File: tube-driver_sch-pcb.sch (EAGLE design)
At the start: 119 parts, among them CN1 KS 54, CN2 MINI B USB, CN3 KS 54, CN4 KS 54, CN5 KS 54, CN6 KS 54, CN7 KS 54, CN8 KS 54, CN9 KS 54, Q4 MMBT3904, Q5 MMBT3904, SW1 RA SM TACT, U1 CP2102, U10 TPS61500, U11 3.3V BUCK, U2 TPS61500, U3 TPS61500, U5 ESP32, U6 USBLC6-2SC6, U8 TPS61500

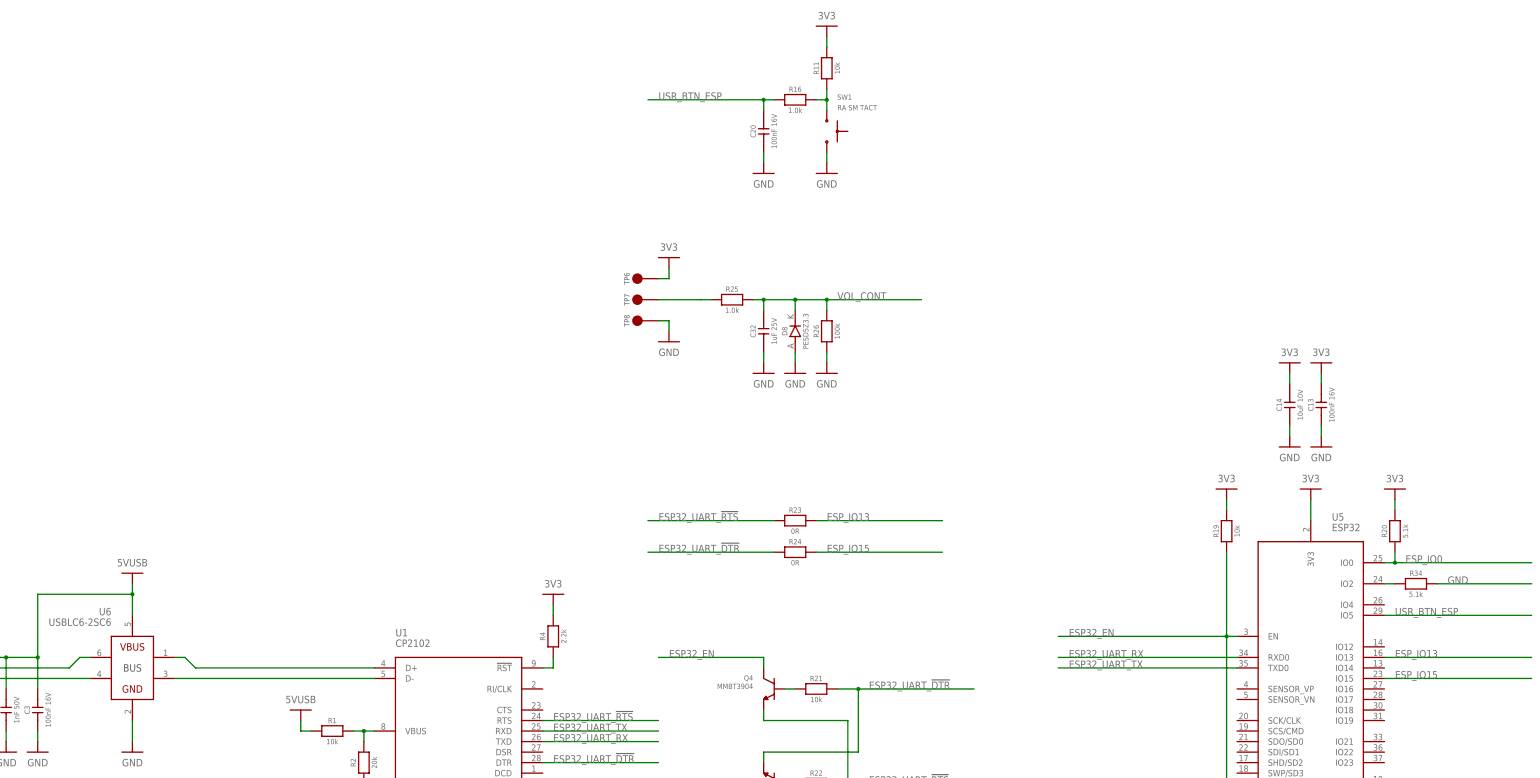
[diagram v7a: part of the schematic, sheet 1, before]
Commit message: Routed and passes DRC
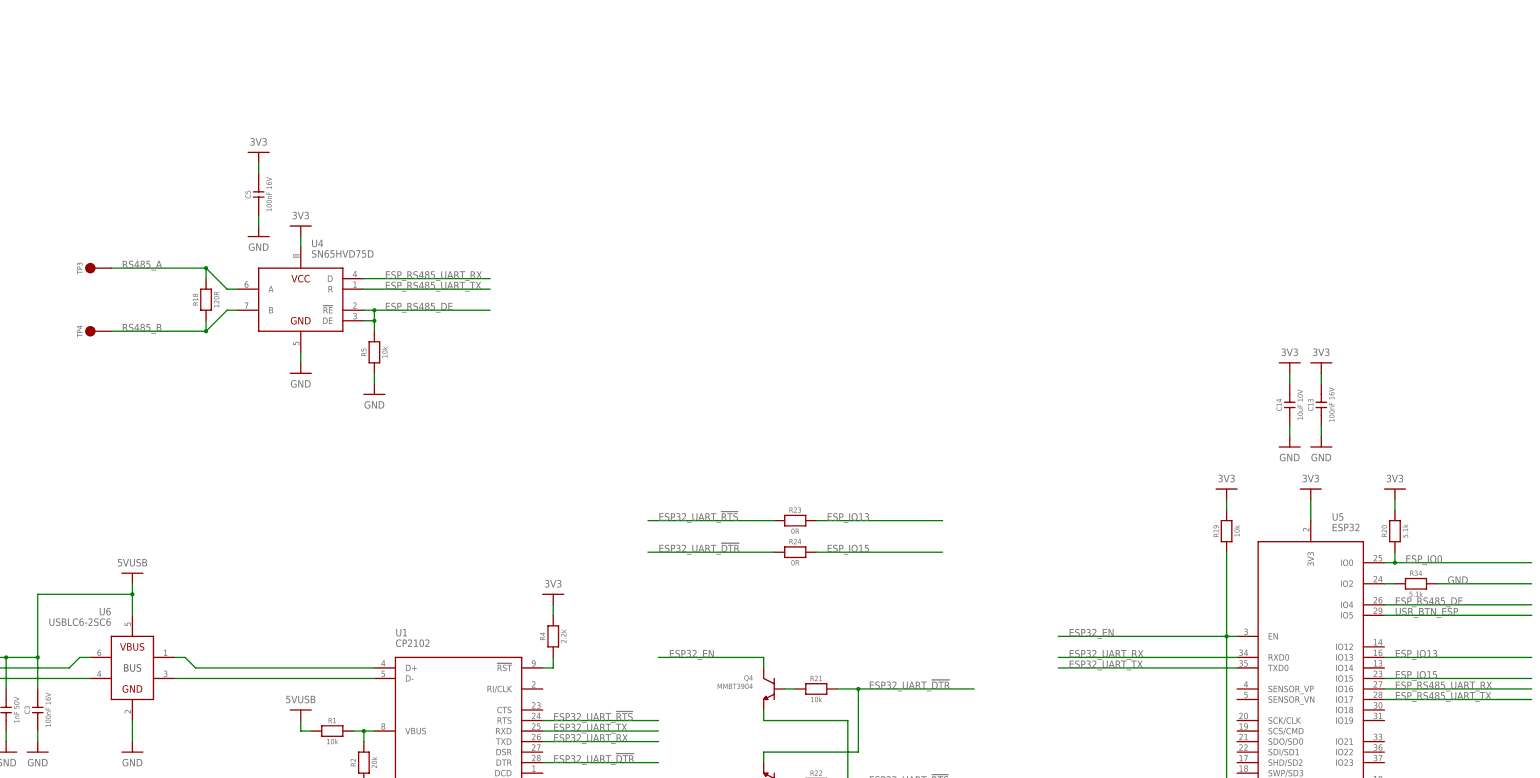
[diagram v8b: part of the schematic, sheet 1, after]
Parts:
- removed C20: 100nF 16V, CAPACITORS:CL10B104KO8WPNC
- removed C32: 1uF 25V, CAPACITORS:CL10A105KA8NNNC
- removed D8: PESD5Z3.3, DIODES:PESD5Z3.3
- removed R11: 10k, r_0603:ERJ3EKF1002V
- removed R16, R25: 1.0k, r_0603:ERJ3EKF1001V
- removed R26: 100k, r_0603:ERJ3EKF1003V
- removed SW1: RA SM TACT, ELECTROMECH:EVQ-P7J01P
- removed TP6, TP7, TP8: 2MM_TEST_POINT, MISC:2MM_TEST_POINT
- added C5: 100nF 16V, CAPACITORS:CL10B104KO8WPNC
- added R18: 120R, r_0603:ERJ3EKF1200V
- added R5: 10k, r_0603:ERJ3EKF1002V
- added TP3, TP4: 2MM_TEST_POINT, MISC:2MM_TEST_POINT
- added U4: SN65HVD75D, ICs:SN65HVD75D
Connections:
- removed net N$4: R25.1, TP7.P$1
- removed net N$85: R11.1, R16.2, SW1.1
- removed net VOL_CONT: C32.2, D8.K, R25.2, R26.2
- new net ESP_RS485_DE: R5.2, U4.!RE, U4.DE, U5.IO4
- new net ESP_RS485_UART_RX: U4.D, U5.IO16
- new net ESP_RS485_UART_TX: U4.R, U5.IO17
- new net RS485_A: R18.2, TP3.P$1, U4.A
- new net RS485_B: R18.1, TP4.P$1, U4.B
- net 3V3: now also C5.2, U4.VCC; no longer R11.2, TP6.P$1
- net GND: now also C5.1, R5.1, U4.GND; no longer C20.1, C32.1, D8.A, R26.1, SW1.2, TP8.P$1
- net USR_BTN_ESP: no longer C20.2, R16.1
